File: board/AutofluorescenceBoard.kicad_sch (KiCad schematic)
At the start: 0 parts

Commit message: Added PAM2863ECR Symbol
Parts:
- added U1: PAM2863ECR, SOIC_863ECR_DIO, symbol 2025-10-08_01-46-07:PAM2863ECR
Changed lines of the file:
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@@
 	(generator_version "9.0")
 	(paper "A4")
+	(symbol
+		(lib_id "2025-10-08_01-46-07:PAM2863ECR")
+		(at 120.65 95.25 0)
+		(unit 1)
+		(exclude_from_sim no)
+		(in_bom yes)
+		(on_board yes)
+		(dnp no)
+		(fields_autoplaced yes)
+		(property "Reference" "U1"
+			(at 143.51 85.09 0)
+			(effects
+				(font
+					(size 1.524 1.524)
+				)
+			)
+		)
+		(property "Value" "PAM2863ECR"
+			(at 143.51 87.63 0)
+			(effects
+				(font
+					(size 1.524 1.524)
+				)
+			)
+		)
+		(property "Footprint" "SOIC_863ECR_DIO"
+			(at 120.65 95.25 0)
+			(effects
+				(font
+					(size 1.27 1.27)
+					(italic yes)
+				)
+				(hide yes)
+			)
+		)
+		(property "Datasheet" "PAM2863ECR"
+			(at 120.65 95.25 0)
+			(effects
+				(font
+					(size 1.27 1.27)
+					(italic yes)
+				)
+				(hide yes)
+			)
+		)
+		(property "Description" ""
+			(at 120.65 95.25 0)
+			(effects
+				(font
+					(size 1.27 1.27)
+				)
+				(hide yes)
+			)
+		)
+		(pin "1"
+		)
+		(pin "2"
+		)
+		(pin "3"
+		)
+		(pin "4"
+		)
+		(pin "EPAD"
+		)
+		(pin "8"
+		)
+		(pin "7"
+		)
+		(pin "6"
+		)
+		(pin "5"
+		)
+		(instances
+			(project ""
+				(path "/5b389890-df33-4c7e-a85b-dd964c46cf24"
+					(reference "U1")
+					(unit 1)
+				)
+			)
+		)
+	)
 	(sheet_instances
 		(path "/"

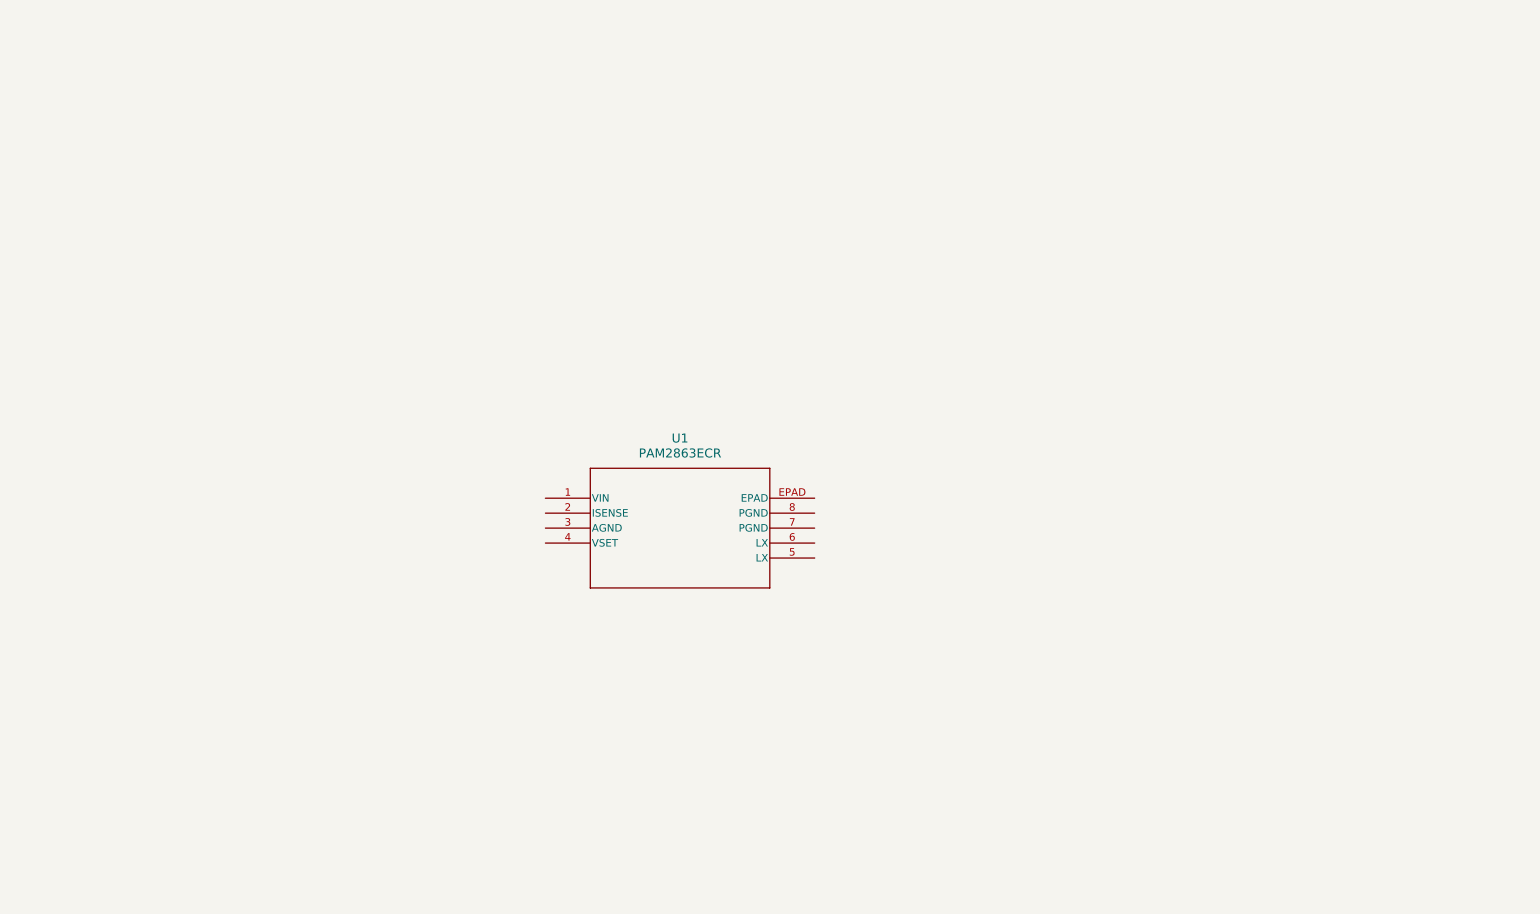
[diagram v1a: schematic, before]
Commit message: First Draft of LED Drivers
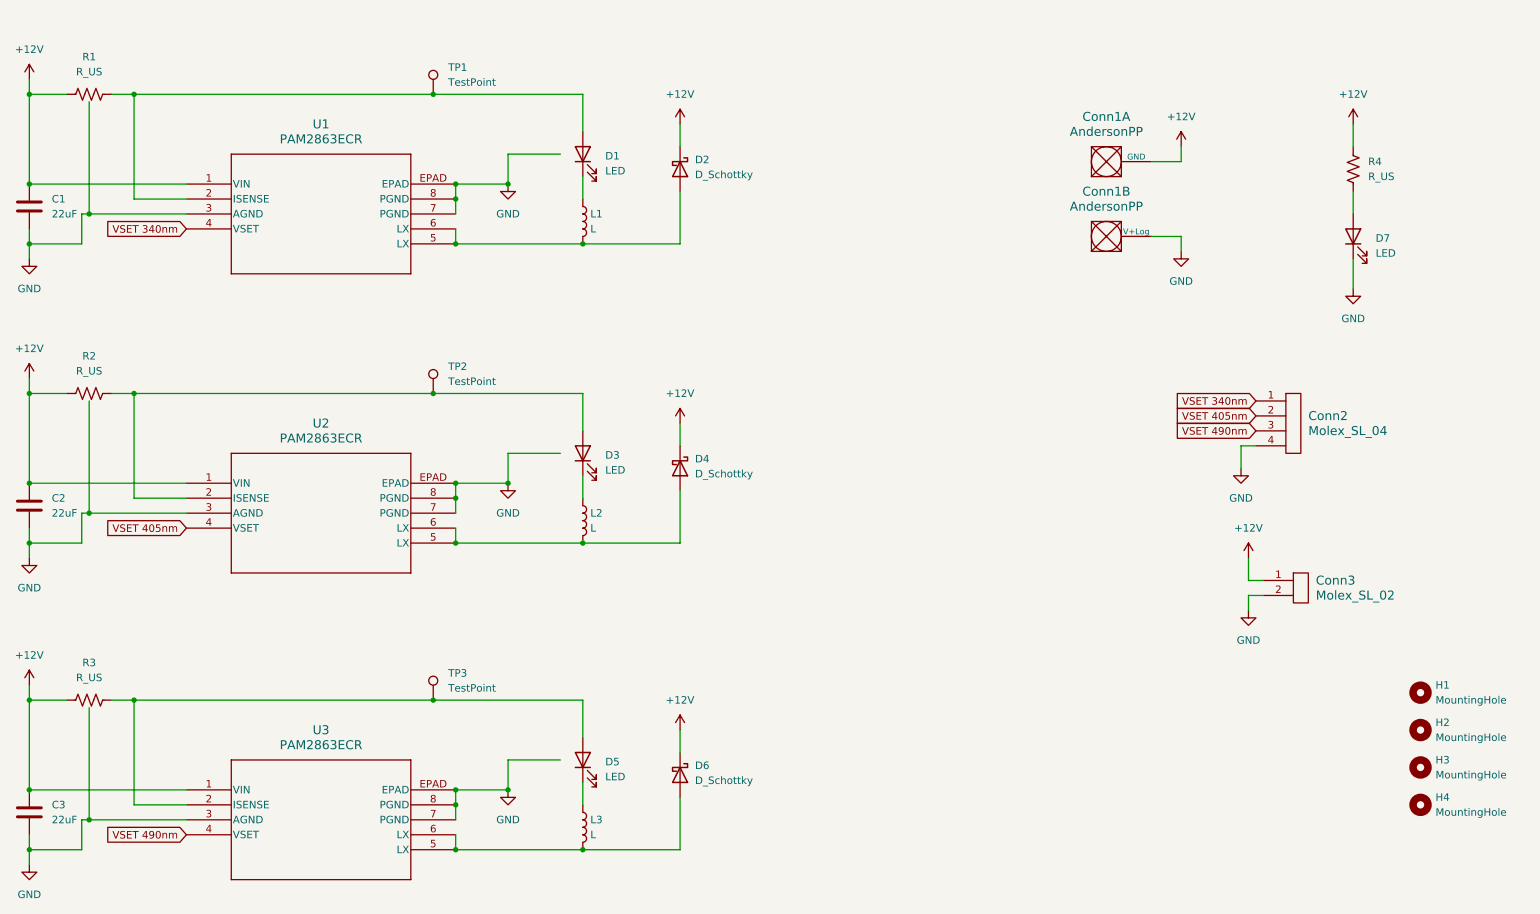
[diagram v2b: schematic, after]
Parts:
- added C1, C2, C3: 22uF, symbol Device:C
- added Conn1: AndersonPP, symbol MRDT_Connectors:AndersonPP
- added Conn2: Molex_SL_04, symbol MRDT_Connectors:Molex_SL_04
- added Conn3: Molex_SL_02, symbol MRDT_Connectors:Molex_SL_02
- added D1, D3, D5, D7: LED, symbol Device:LED
- added D2, D4, D6: D_Schottky, symbol Device:D_Schottky
- added H1, H2, H3, H4: MountingHole, symbol Mechanical:MountingHole
- added L1, L2, L3: L, symbol Device:L
- added R1, R2, R3, R4: R_US, symbol Device:R_US
- added TP1, TP2, TP3: TestPoint, symbol Connector:TestPoint
- added U2, U3: PAM2863ECR, SOIC_863ECR_DIO, symbol 2025-10-08_01-46-07:PAM2863ECR
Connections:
- net +12V: now reaches U1.1 (VIN)
- net +12V: now also C1.1, C2.1, C3.1, Conn1.1 (GND), Conn3.1, D2.1 (K), D4.1 (K), D6.1 (K), R1.1, R2.1, R3.1, R4.1, U2.1 (VIN), U3.1 (VIN)
- net at U1.2 (ISENSE): now also D1.2 (A), R1.2, TP1.1
- net GND: now reaches U1.3 (AGND)
- net GND: now also U1.7 (PGND), U1.8 (PGND), U1.EPAD, C1.2, C2.2, C3.2, Conn1.2 (V+Log), Conn2.4, Conn3.2, D7.1 (K), U2.3 (AGND), U2.7 (PGND), U2.8 (PGND), U2.EPAD, U3.3 (AGND), U3.7 (PGND), U3.8 (PGND), U3.EPAD
- net VSET 340nm: now reaches U1.4 (VSET)
- net VSET 340nm: now also Conn2.1
- net at U1.5 (LX): now also U1.6 (LX), D2.2 (A), L1.2
- new net: D7.2 (A), R4.2
- new net: D5.2 (A), R3.2, TP3.1, U3.2 (ISENSE)
- new net: D6.2 (A), L3.2, U3.5 (LX), U3.6 (LX)
- new net: D3.2 (A), R2.2, TP2.1, U2.2 (ISENSE)
- new net: D4.2 (A), L2.2, U2.5 (LX), U2.6 (LX)
- new net: D3.1 (K), L2.1
- new net: D1.1 (K), L1.1
- new net: D5.1 (K), L3.1
- new net VSET 405nm: Conn2.2, U2.4 (VSET)
- new net VSET 490nm: Conn2.3, U3.4 (VSET)
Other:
- moved on the sheet: U1

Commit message: Edited Components
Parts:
- removed D1, D3, D5: LED, symbol Device:LED
- removed R1, R2, R3: R_US, symbol Device:R_US
- added D1: 405nm, symbol AutofluorescenceBoard:LED_GNDPad
- added D3: 340nm, symbol AutofluorescenceBoard:LED_GNDPad
- added D5: 490nm, symbol AutofluorescenceBoard:LED_GNDPad
- added U1, U2, U3: 0.1R, symbol AutofluorescenceBoard:R_2
- L1, L2, L3: value L -> 47uH
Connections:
- net +12V: now also U1., U2., U3.
- net GND: now also D1.3, D3.3, D5.3, U1., U2., U3.
- net at TP3.1, U3.2 (ISENSE): now also D5.2, U3.
- net at TP2.1, U2.2 (ISENSE): now also D1.2, U2.
- net at TP1.1, U1.2 (ISENSE): now also D3.2, U1.
- net at L2.1: now also D1.1
- net at L1.1: now also D3.1
- net at L3.1: now also D5.1

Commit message: Added Some Footprints
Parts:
- Conn1: footprint (none) -> MRDT_Connectors:Square_Anderson_2_H_Side_By_Side
- Conn2: footprint (none) -> MRDT_Connectors:MOLEX_SL_04_Horizontal
- Conn3: footprint (none) -> MRDT_Connectors:MOLEX_SL_02_Horizontal
- D7: footprint (none) -> LED_SMD:LED_0603_1608Metric_Pad1.05x0.95mm_HandSolder
- H1, H2, H3, H4: footprint (none) -> MountingHole:MountingHole_3.5mm
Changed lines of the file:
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@@
 			)
 		)
-		(property "Footprint" ""
+		(property "Footprint" "LED_SMD:LED_0603_1608Metric_Pad1.05x0.95mm_HandSolder"
 			(at 257.81 50.8 0)
 			(effects
@@
 			)
 		)
-		(property "Datasheet" "PAM2863ECR"
+		(property "Datasheet" "https://www.diodes.com/assets/Datasheets/PAM2863.pdf"
 			(at 59.69 144.78 0)
 			(effects
@@
 			)
 		)
-		(property "Datasheet" "PAM2863ECR"
+		(property "Datasheet" "https://www.diodes.com/assets/Datasheets/PAM2863.pdf"
 			(at 59.69 92.71 0)
 			(effects
@@
 			)
 		)
-		(property "Footprint" ""
+		(property "Footprint" "MRDT_Connectors:Square_Anderson_2_H_Side_By_Side"
 			(at 209.55 54.61 0)
 			(effects
@@
 			)
 		)
-		(property "Datasheet" "PAM2863ECR"
+		(property "Datasheet" "https://www.diodes.com/assets/Datasheets/PAM2863.pdf"
 			(at 59.69 41.91 0)
 			(effects
@@
 			)
 		)
-		(property "Footprint" ""
+		(property "Footprint" "MountingHole:MountingHole_3.5mm"
 			(at 269.24 140.97 0)
 			(effects
@@
 			)
 		)
-		(property "Footprint" ""
+		(property "Footprint" "MountingHole:MountingHole_3.5mm"
 			(at 269.24 134.62 0)
 			(effects
@@
 			)
 		)
-		(property "Footprint" ""
+		(property "Footprint" "MRDT_Connectors:MOLEX_SL_04_Horizontal"
 			(at 246.38 87.63 0)
 			(effects
@@
 			)
 		)
-		(property "Footprint" ""
+		(property "Footprint" "MountingHole:MountingHole_3.5mm"
 			(at 269.24 147.32 0)
 			(effects
@@
 			)
 		)
-		(property "Footprint" ""
+		(property "Footprint" "MRDT_Connectors:MOLEX_SL_02_Horizontal"
 			(at 247.65 115.57 0)
 			(effects
@@
 			)
 		)
-		(property "Footprint" ""
+		(property "Footprint" "MountingHole:MountingHole_3.5mm"
 			(at 269.24 128.27 0)
 			(effects
@@
 			)
 		)
-		(property "Footprint" ""
+		(property "Footprint" "MRDT_Connectors:Square_Anderson_2_H_Side_By_Side"
 			(at 209.55 67.31 0)
 			(effects

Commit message: Changed Led 365
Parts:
- D3: value 340nm -> 365nm
- R4: value R_US -> 2.2k
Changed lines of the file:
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@@
 			)
 		)
-		(property "Value" "340nm"
+		(property "Value" "365nm"
 			(at 132.08 36.8299 0)
 			(effects
@@
 			)
 		)
-		(property "Datasheet" ""
+		(property "Datasheet" "https://mm.digikey.com/Volume0/opasdata/d220001/medias/docus/320/ELUA3535OGB_Series_Rev2_1-24-19.pdf"
 			(at 127 36.83 0)
 			(effects
@@
 			)
 		)
-		(property "Value" "R_US"
+		(property "Value" "2.2k"
 			(at 260.35 40.6399 0)
 			(effects
@@
 			)
 		)
-		(property "Datasheet" ""
+		(property "Datasheet" "http://www.s-et.com/upload2/CUN06B1B_181016_R9.4.pdf"
 			(at 127 87.63 0)
 			(effects

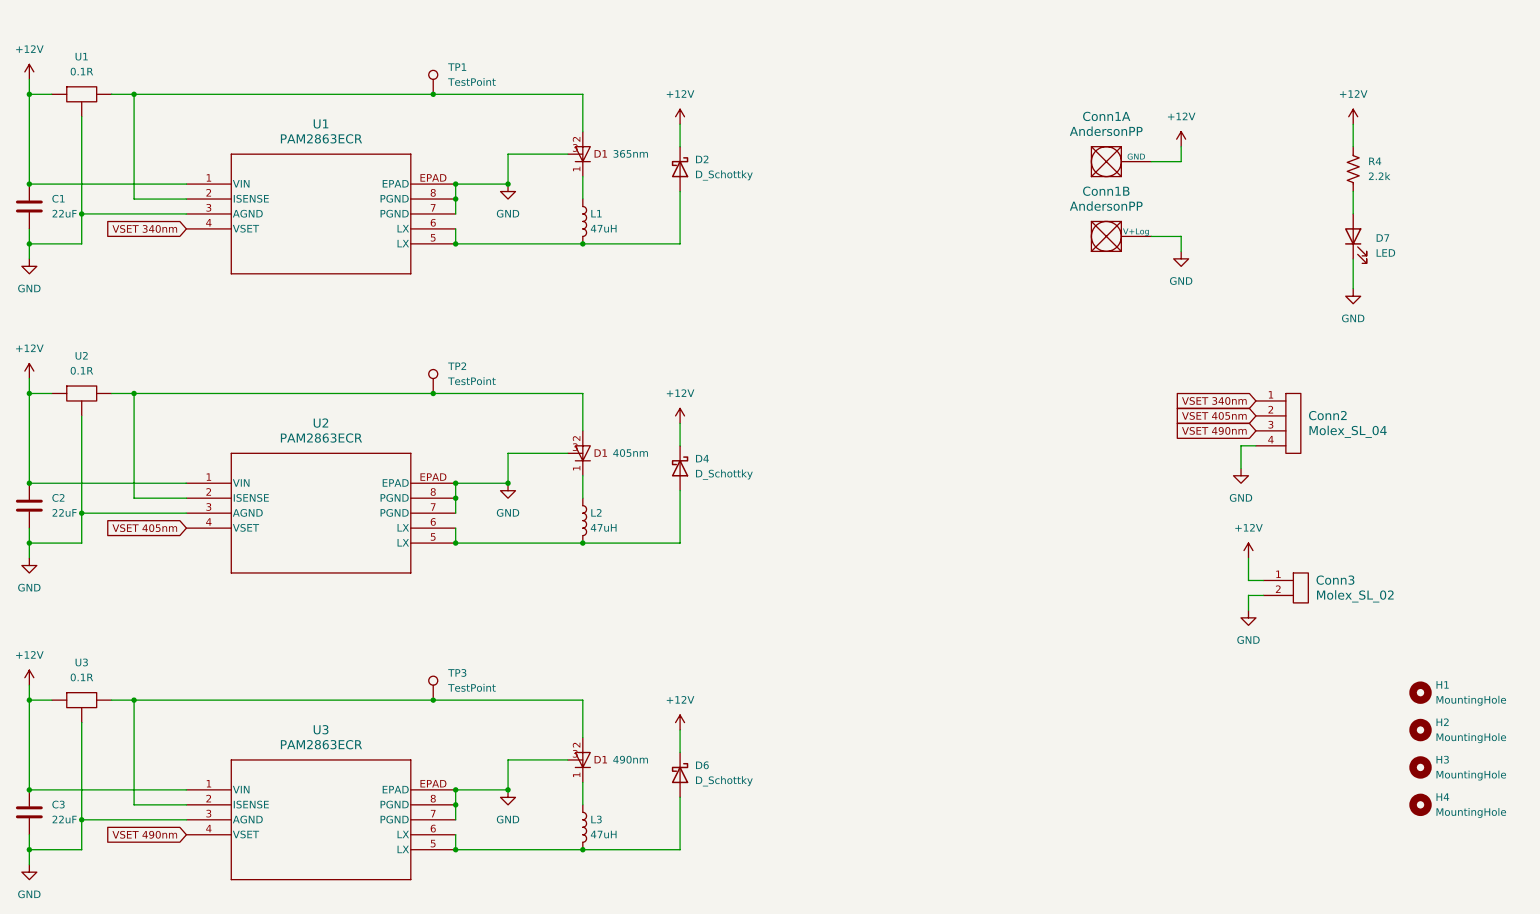
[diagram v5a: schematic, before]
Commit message: Added Rev.1 Mods, Datasheets and Footprints
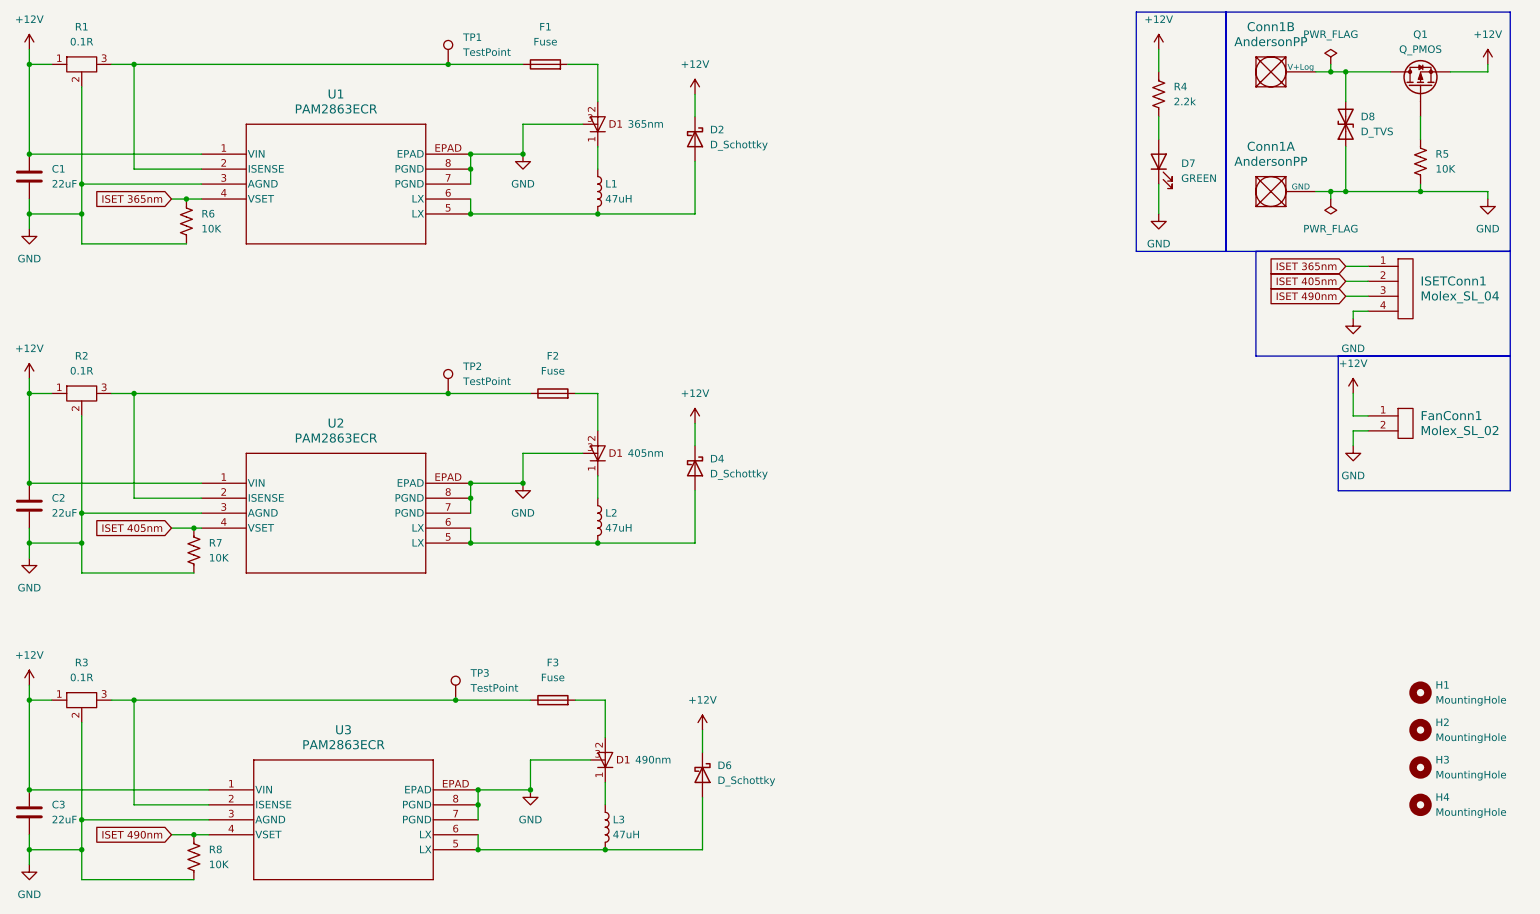
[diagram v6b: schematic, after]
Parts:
- added D8: D_TVS, ESDALC14-1BF4:ESDALC14-1BF4, symbol Device:D_TVS
- added F1, F2, F3: Fuse, Fuse:Fuse_0603_1608Metric, symbol Device:Fuse
- added Q1: Q_PMOS, AF Board:P-MOSFET, symbol Device:Q_PMOS
- added R5, R6, R7, R8: 10K, AF Board:RES_R0603_ROM-L, symbol Device:R_US
- C1, C2, C3: footprint (none) -> AF Board:CAP_CL_21_SAM-L
- D2, D4, D6: footprint (none) -> AF Board:Schottky
- D7: value LED -> GREEN
- L1, L2, L3: footprint (none) -> AF Board:Inductor
- R1: renamed from U1; footprint (none) -> AF Board:TO508P1229X317-3N
- R2: renamed from U2; footprint (none) -> AF Board:TO508P1229X317-3N
- R3: renamed from U3; footprint (none) -> AF Board:TO508P1229X317-3N
- R4: footprint (none) -> AF Board:2.2K Res
- TP1, TP2, TP3: footprint (none) -> TestPoint:TestPoint_Pad_D1.5mm
- U1, U2, U3: footprint SOIC_863ECR_DIO -> AF Board:LED_IC
- renumbered Conn3 to FanConn1, Conn2 to ISETConn1
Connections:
- net +12V: now also R1.1, R2.1, R3.1, Q1.S; no longer Conn1.1 (GND), R1., R2., R3.
- net GND: now also Conn1.1 (GND), R1.2, R2.2, R3.2, D8.1 (A1), R5.2, R6.2, R7.2, R8.2; no longer Conn1.2 (V+Log), R1., R2., R3.
- net at TP3.1, U3.2 (ISENSE): now also R3.3, F3.1; no longer D5.2, R3.
- net at TP2.1, U2.2 (ISENSE): now also R2.3, F2.1; no longer D1.2, R2.
- net at TP1.1, U1.2 (ISENSE): now also R1.3, F1.1; no longer D3.2, R1.
- net VSET 340nm renamed ISET 365nm
- net ISET 365nm: now also R6.1
- net VSET 405nm renamed ISET 405nm
- net ISET 405nm: now also R7.1
- net VSET 490nm renamed ISET 490nm
- net ISET 490nm: now also R8.1
- new net: D3.2, F1.2
- new net: D1.2, F2.2
- new net: D5.2, F3.2
- new net: Conn1.2 (V+Log), D8.2 (A2), Q1.D
- new net: Q1.G, R5.1
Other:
- moved on the sheet: C1, Conn1A, Conn1B, D2, D4, D6, D7, FanConn1, ISETConn1, L1, L2, L3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
